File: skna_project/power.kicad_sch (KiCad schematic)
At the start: 19 parts, among them J1 Screw_Terminal_01x02, J3 USB_B_Micro, Q1 AO3401A, U2 MP2359DJ-LF-Z, U2 USBLC6-2SC6

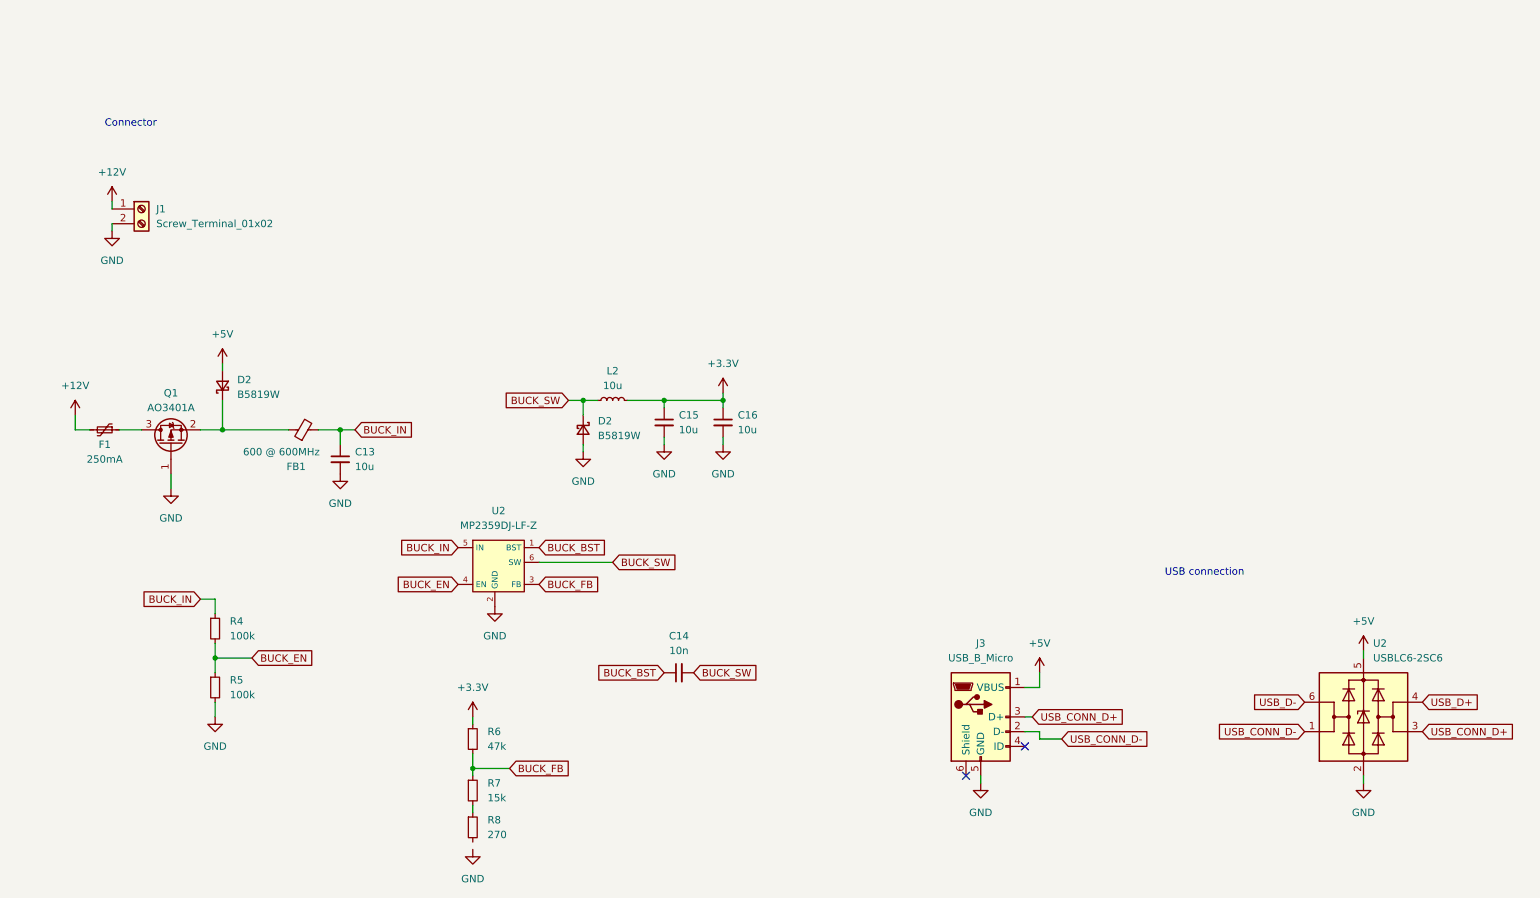
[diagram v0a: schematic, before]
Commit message: added flash drive to circuit
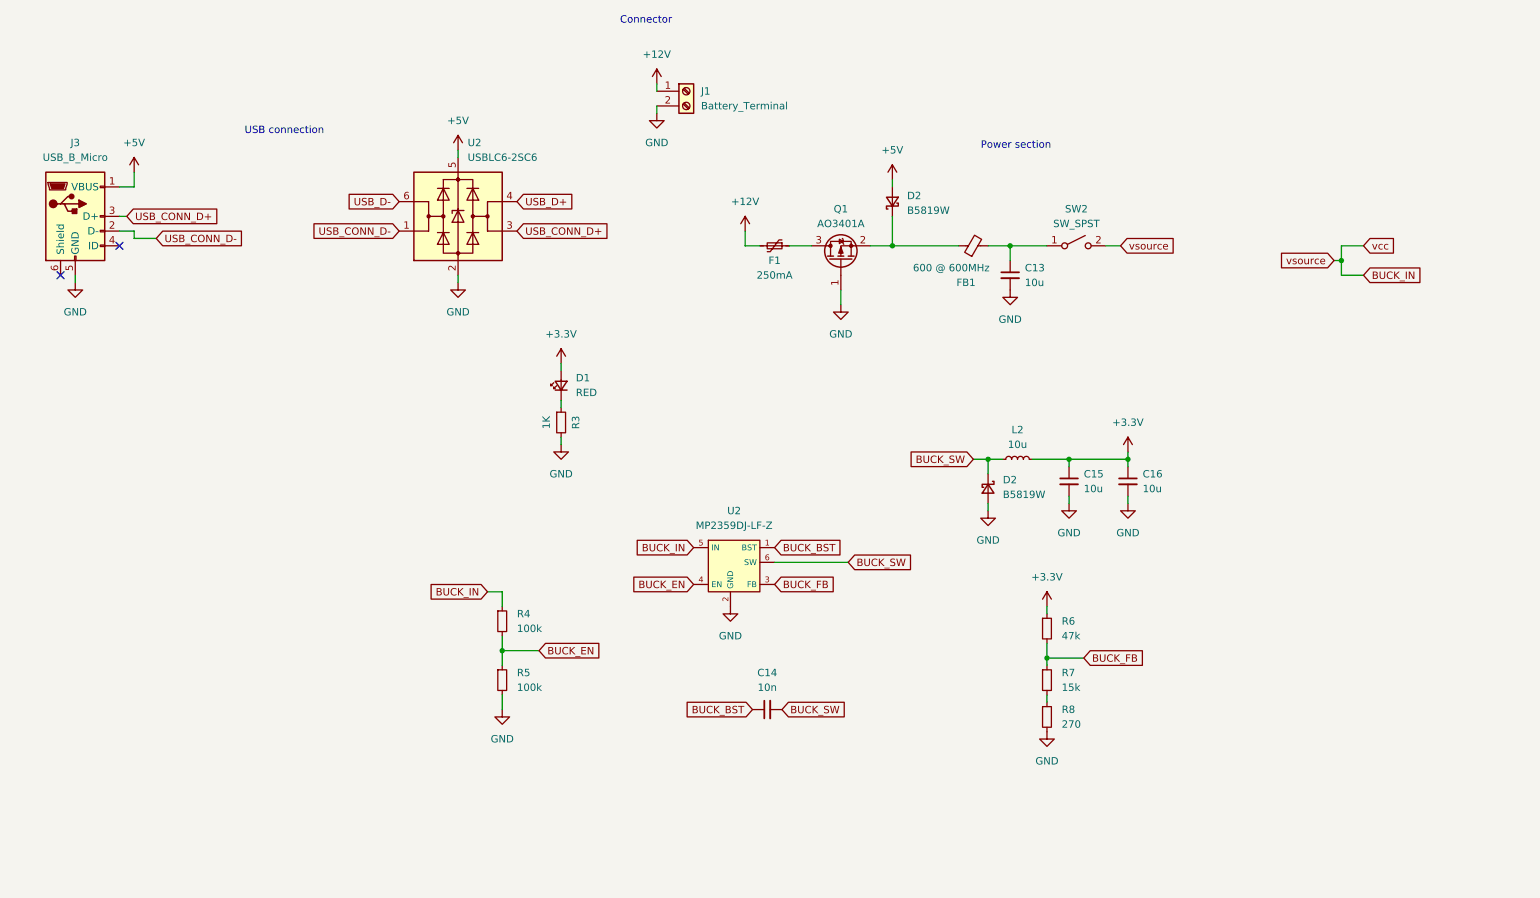
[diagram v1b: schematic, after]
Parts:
- added D1: RED, symbol Device:LED_Small
- added R3: 1K, symbol Device:R_Small
- added SW2: SW_SPST, symbol Switch:SW_SPST
- J1: value Screw_Terminal_01x02 -> Battery_Terminal
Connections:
- net +3.3V: now also D1.2 (A)
- net BUCK_IN: now also SW2.2 (B); no longer C13.1, FB1.2
- net GND: now also R8.2, R3.2
- new net: D1.1 (K), R3.1
- new net: C13.1, FB1.2, SW2.1 (A)
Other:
- note added: "Power section"
- moved on the sheet: C13, C14, C15, C16, D2, F1, FB1, J1, J3, L2, Q1, R4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

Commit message: Replaced ADS129 with ADS8232
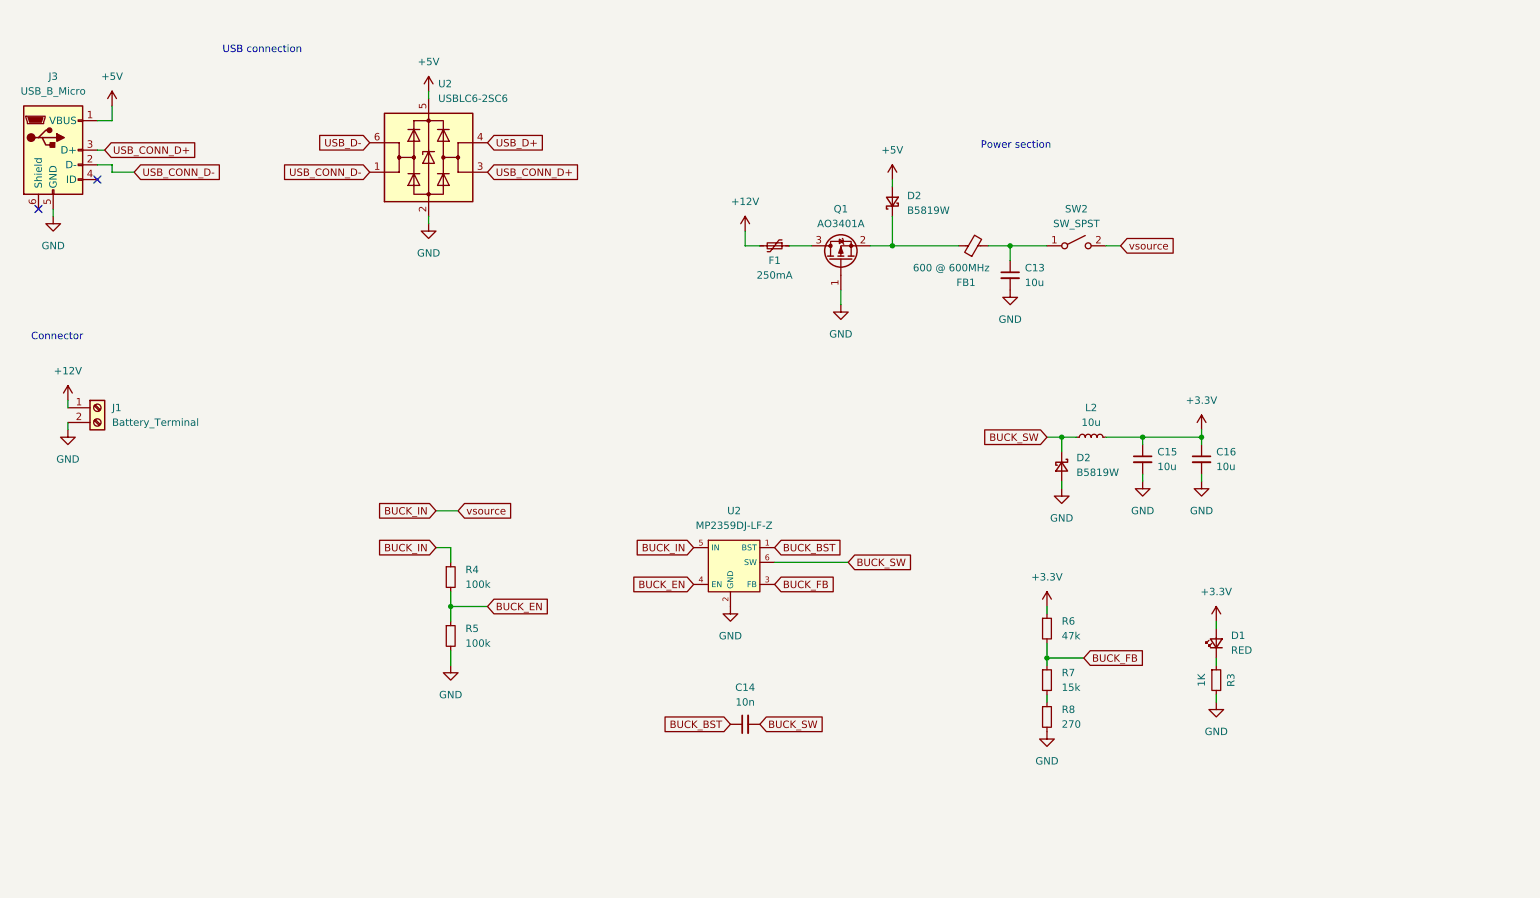
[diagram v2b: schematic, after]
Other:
- moved on the sheet: C14, C15, C16, D1, D2, J1, J3, L2, R3, R4, R5, U2
